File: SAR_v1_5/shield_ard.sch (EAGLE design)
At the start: 14 parts

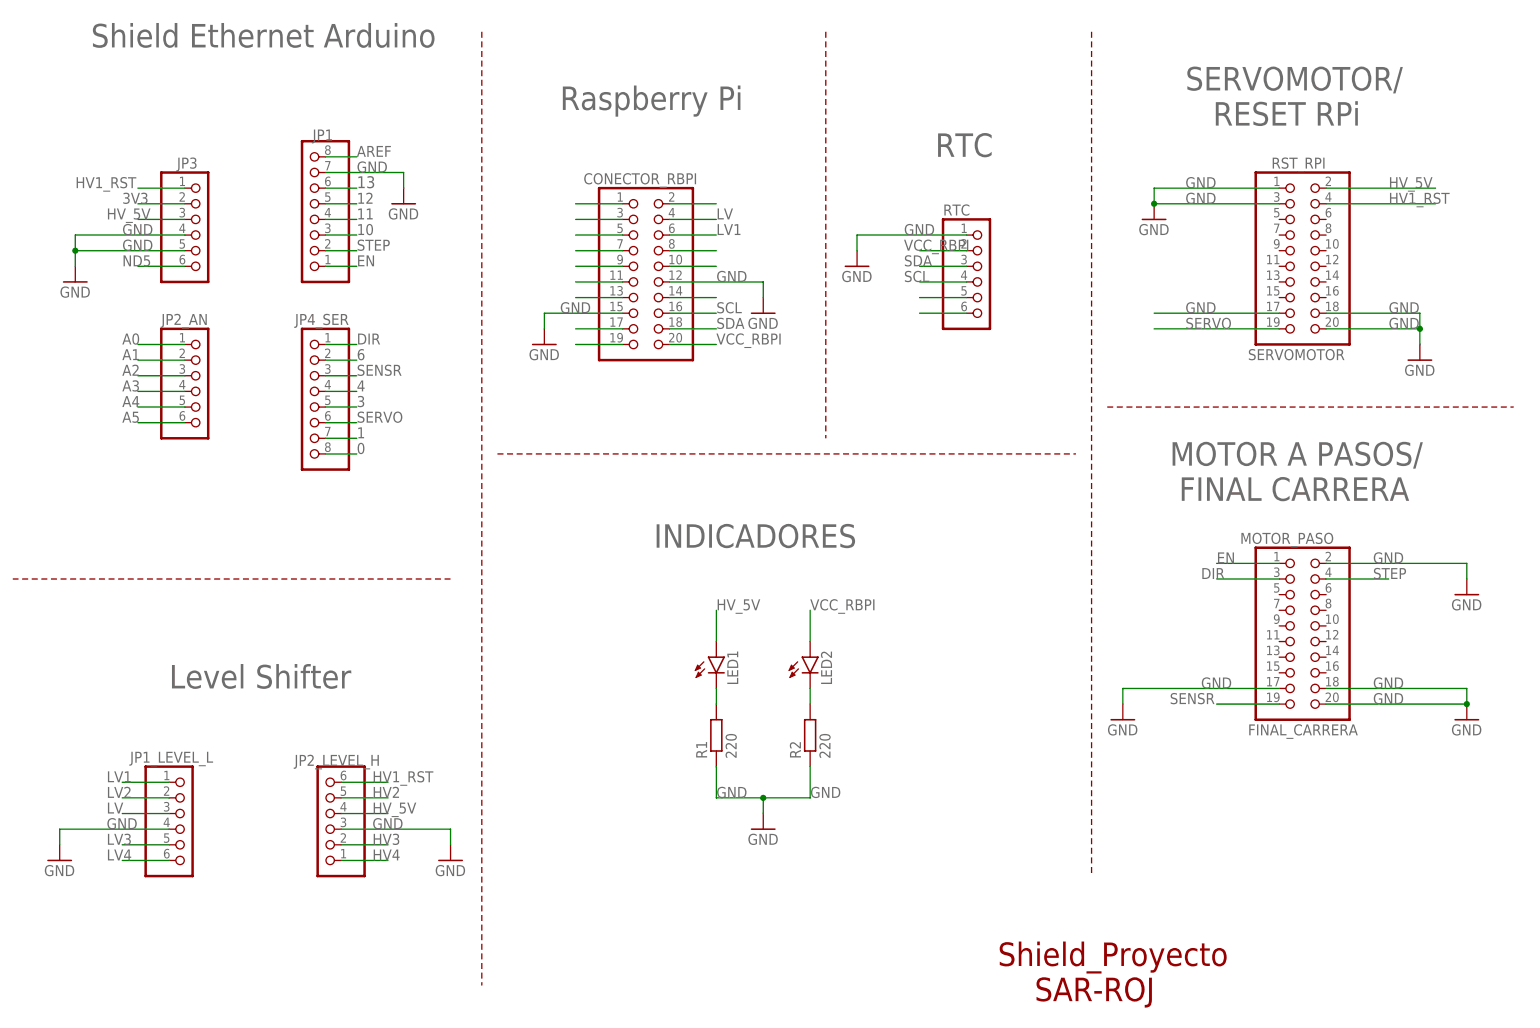
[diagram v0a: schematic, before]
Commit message: many componentes were placed in other position on the board
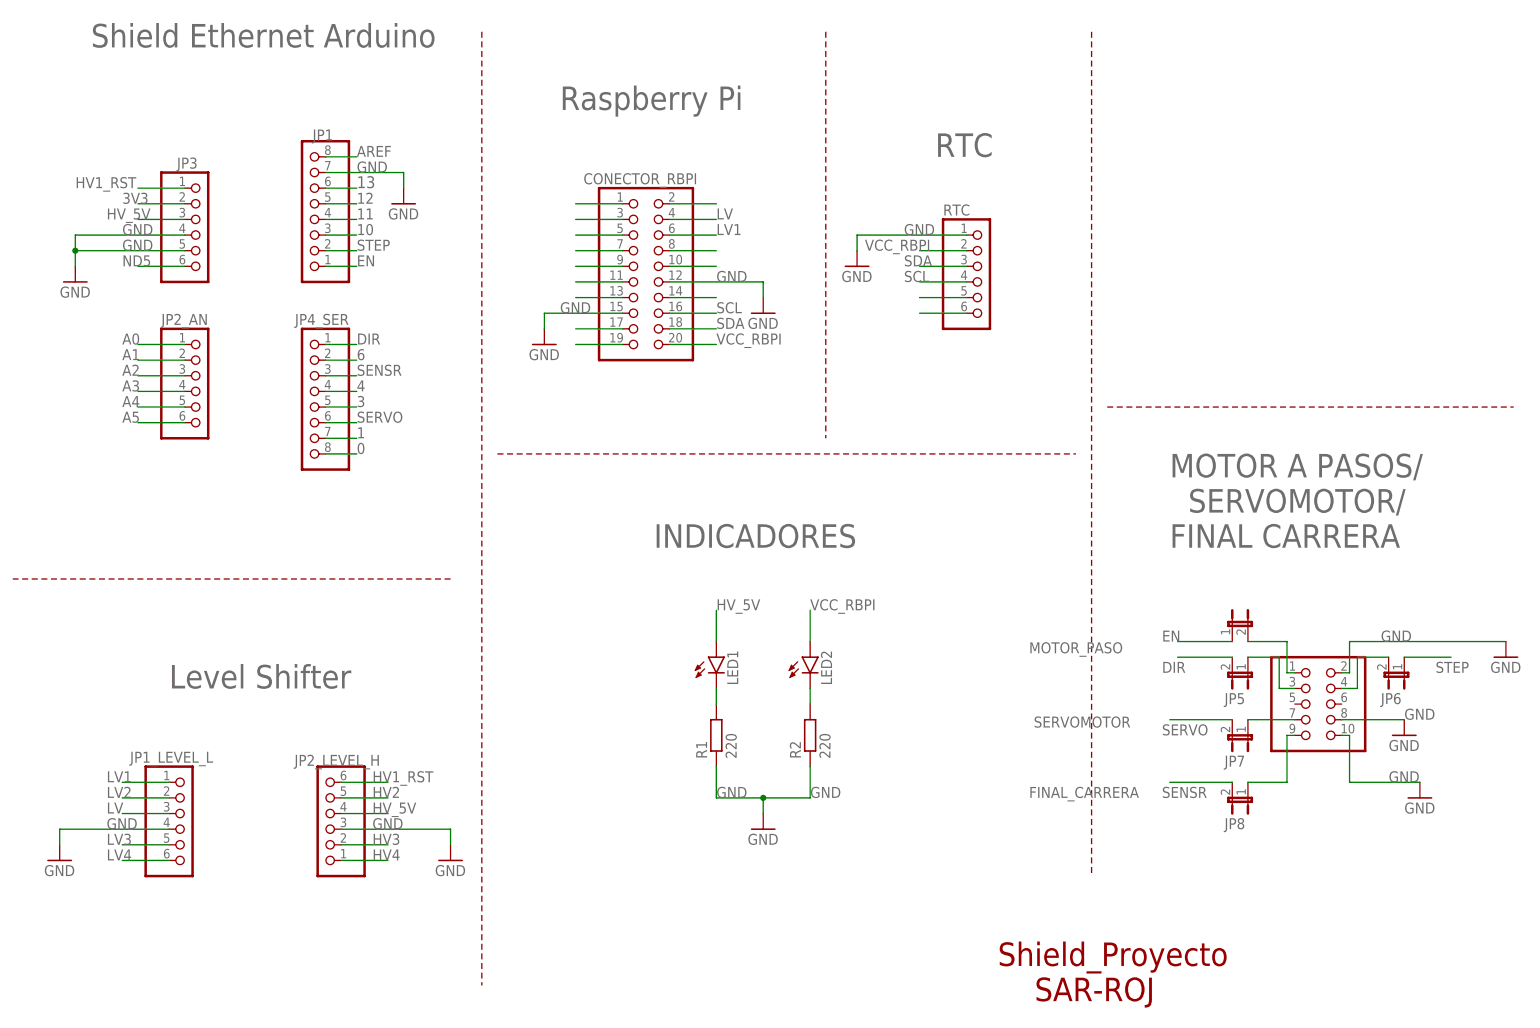
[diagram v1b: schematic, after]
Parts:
- removed RST_RPI: (no value), pinhead:PINHD-2X10
- added JP2, JP5, JP6, JP7, JP8: (no value), SparkFun-Retired:JUMPER-2PTH
- MOTOR_PASO: device pinhead:PINHD-2X10 -> pinhead:PINHD-2X5
- RTC: device pinhead:PINHD-1X6 -> pinhead:PINHD-1X6/90
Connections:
- new net N$6: JP6.2, MOTOR_PASO.4
- new net N$7: JP7.1, MOTOR_PASO.7
- net DIR: now also JP5.1, JP5.2
- net EN: now also JP2.1, JP2.2
- net GND: now also MOTOR_PASO.10, MOTOR_PASO.8; no longer MOTOR_PASO.17, MOTOR_PASO.18, MOTOR_PASO.20, RST_RPI.1, RST_RPI.17, RST_RPI.18, RST_RPI.20, RST_RPI.3
- net HV1_RST: no longer RST_RPI.4
- net HV_5V: no longer RST_RPI.2
- net SENSR: now also JP8.1, JP8.2, MOTOR_PASO.9; no longer MOTOR_PASO.19
- net SERVO: now also JP7.2; no longer RST_RPI.19
- net STEP: now also JP6.1; no longer MOTOR_PASO.4
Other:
- note added: "MOTOR A PASOS/ SERVOMOTOR/ FINAL CARRERA"
- note removed: "MOTOR A PASOS/ FINAL CARRERA"
- note removed: "SERVOMOTOR/ RESET RPi"
